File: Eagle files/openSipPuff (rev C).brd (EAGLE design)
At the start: 30.1 x 58.7 mm, 20 parts, among them J2 1X04-RA, J3 AVR_SPI_PRG_62X3_LOCK, U1 ATMEGA32U4TQFP, U2 AD8223, U3 MPX12GP, Y1 16MHz

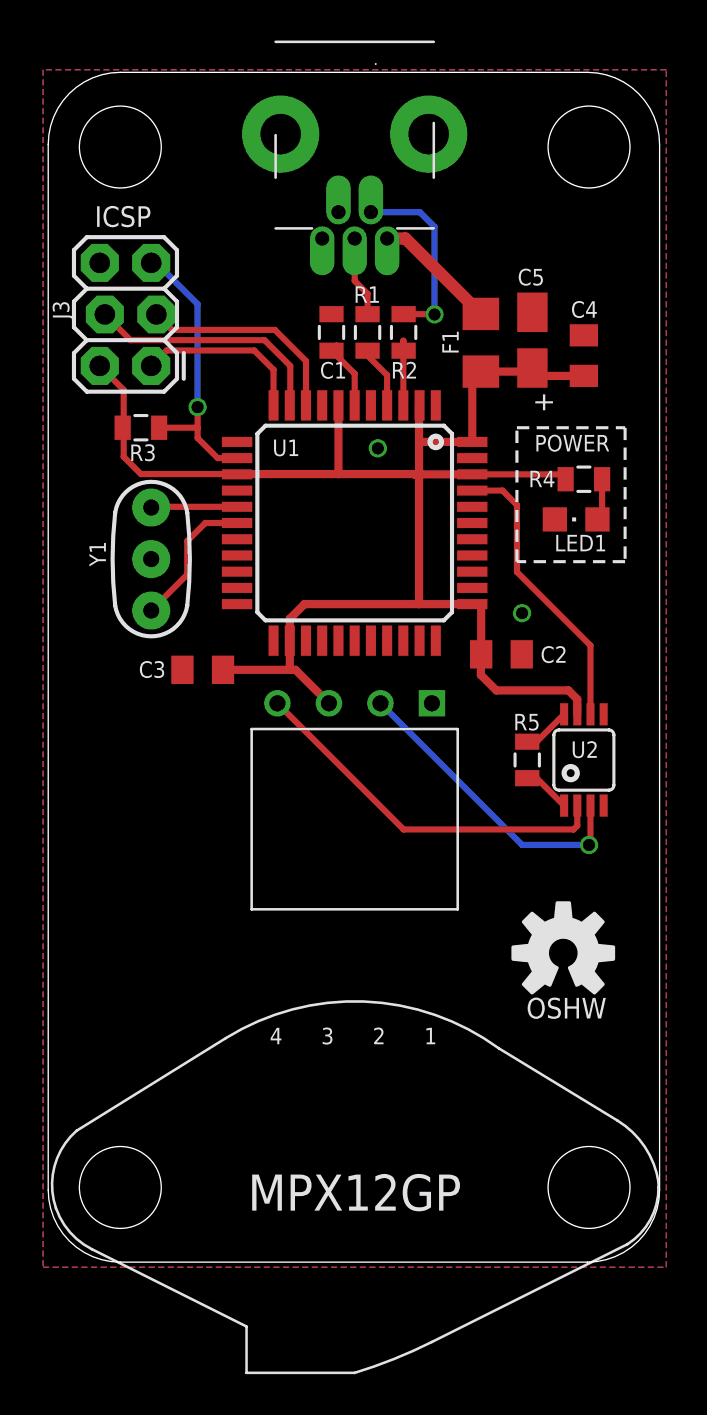
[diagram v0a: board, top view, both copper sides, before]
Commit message: Rev C updates
New Eagle files and BOM.
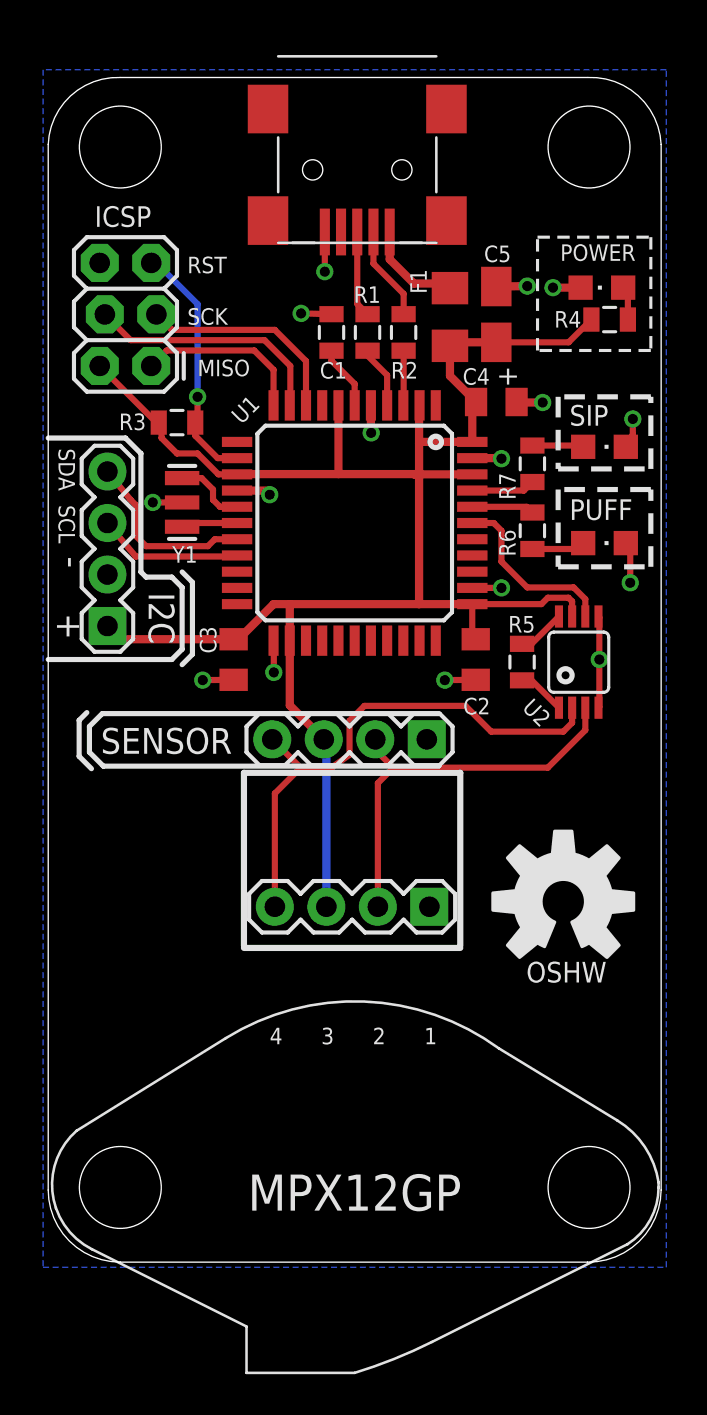
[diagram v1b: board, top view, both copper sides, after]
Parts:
- removed CN1: (no value), adafruit:USB-MINIB-THM-MOLEX
- added CN2: (no value), adafruit:USB-MINIB
- added LED2: RED, led:CHIPLED_0805
- added LED3: BLUE, led:CHIPLED_0805
- added R6, R7: 82, SparkFun-Resistors:0805
- added SENSOR, SENSOR1: (no value), SparkFun-Connectors:1X04
- J2: value 1X04-RA -> I2C; device sip-and-puff:1X04-RA -> SparkFun-Connectors:1X04
- LOGO1: value OSHW-LOGOM -> OSHW-LOGOL; device SparkFun-Aesthetics:OSHW-LOGO-M -> SparkFun-Aesthetics:OSHW-LOGO-L
- Y1: device SparkFun-FreqCtrl:RESONATOR-PTH -> SparkFun-FreqCtrl:RESONATOR-SMD
- moved J2 15.1 mm to (2.92, 31.4), turned to 90 degrees
- moved LED1 11.5 mm to (27.3, 48.1)
- moved R4 7.98 mm to (27.7, 46.5)
- moved C4 4.89 mm to (22.1, 42.4), turned to 0 degrees
- moved R5 4.83 mm to (23.4, 29.6)
- moved U2 4.83 mm to (26.2, 29.6)
- moved Y1 3.18 mm to (6.60, 37.5)
- moved LOGO1 2.54 mm to (25.4, 17.8)
- moved C5 2.18 mm to (22.1, 46.7)
- moved F1 1.98 mm to (19.8, 46.6)
- moved R3 1.80 mm to (6.35, 41.4)
- moved C3 1.61 mm to (9.14, 29.7), turned to 270 degrees
- moved C2 1.30 mm to (21.1, 29.7), turned to 270 degrees
- renumbered J3 to J1
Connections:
- removed net SENSOR_OUT: U1.41, U2.6
- new net N$14: LED3.A, R7.2
- new net N$15: LED2.A, R6.2
- new net N$8: R6.1, U1.40
- new net N$9: R7.1, U1.41
- new net OUTPUT: U1.39, U2.6
- new net SCL: J2.4, U1.18
- new net SDA: J2.3, U1.19
- net 5V: now also J2.1, SENSOR.3, SENSOR1.3; no longer J2.P$3
- net D+: now also CN2.D+; no longer CN1.D+
- net D-: now also CN2.D-; no longer CN1.D-
- net GND: now also CN2.GND, J2.2, LED2.C, LED3.C, SENSOR.1, SENSOR1.1; no longer CN1.GND, J2.P$1
- net N$10: now also SENSOR.2, SENSOR1.2; no longer J2.P$2
- net N$13: now also SENSOR.4, SENSOR1.4; no longer J2.P$4
- net N$4: now also CN2.VBUS; no longer CN1.VBUS
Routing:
- net GND: track 0.00 -> 27.9 mm, vias 2 -> 16
- net SENSOR_OUT: track 14.3 -> 0.00 mm
- net 5V: track 80.0 -> 92.5 mm
- net SCL: track 0.00 -> 9.04 mm
- net OUTPUT: track 0.00 -> 8.88 mm
- net N$13: track 18.4 -> 26.4 mm
- net SDA: track 0.00 -> 7.18 mm
- net N$10: track 15.2 -> 20.3 mm, vias 1 -> 0
- net D-: track 9.28 -> 4.67 mm, vias 1 -> 0
- net N$5: track 6.99 -> 2.79 mm
- net N$9: track 0.00 -> 3.14 mm
- net N$8: track 0.00 -> 3.08 mm
- net N$14: track 0.00 -> 2.84 mm
- net N$15: track 0.00 -> 2.63 mm
- net RESET: track 14.0 -> 12.5 mm
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- removed copper zone on layer 1, net GND
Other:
- board size 30.1 x 58.7 mm -> 30.2 x 58.4 mm
- board text added: "+"
- board text added: "-"
- board text added: "I2C"
- board text added: "PUFF"
- board text added: "SCL"
- board text added: "SDA"
- board text added: "SIP"
- board text added: "rev C"
- board text removed: "Y1"
- board text removed: "rev B"
